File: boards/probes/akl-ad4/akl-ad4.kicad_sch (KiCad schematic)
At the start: 33 parts, among them J1 U.FL, J2 TIPRES, J3 TIPRES, J4 SMPM, U1 ADP7142ACPZN-R7, U2 ADP7182_DFN8, U3 LMR70503, U4 ADL5569

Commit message: Small tweaks to AKL-AD4 from design review. Ready for fab.
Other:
- company: (none) -> Antikernel Labs
- title: (none) -> AKL-AD4
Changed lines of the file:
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@@
 (kicad_sch (version 20211123) (generator eeschema)
   (paper "A4")
+  (title_block
+    (title "AKL-AD4")
+    (date "2022-06-11")
+    (rev "0.1")
+    (company "Antikernel Labs")
+    (comment 1 "Andrew D. Zonenberg")
+  )
   (junction (at 81.28 64.77) (diameter 0) (color 0 0 0 0)
   )

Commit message: Rev 0.2 of AKL-AD4
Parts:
- R7, R8: footprint azonenberg_pcb:EIA_0402_RES_NOSILK -> azonenberg_pcb:EIA_0201_RES_NOSILK
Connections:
- net 2V5_P: no longer U4.16 (PBDB)
- net GND: now also U4.16 (PBDB)
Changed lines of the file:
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@@
   (title_block
     (title "AKL-AD4")
-    (date "2022-06-11")
-    (rev "0.1")
+    (date "2022-06-24")
+    (rev "0.2")
     (company "Antikernel Labs")
     (comment 1 "Andrew D. Zonenberg")
@@
     (effects (font (size 1.27 1.27)) (justify right bottom))
   )
-  (label "2V5_P" (at 196.85 134.62 180)
+  (label "GND" (at 196.85 134.62 180)
     (effects (font (size 1.27 1.27)) (justify right bottom))
   )
@@
     (property "Reference" "R7" (id 0) (at 171.45 127 90))
     (property "Value" "348" (id 1) (at 171.45 129.54 90))
-    (property "Footprint" "azonenberg_pcb:EIA_0402_RES_NOSILK" (id 2) (at 171.45 131.318 90)
+    (property "Footprint" "azonenberg_pcb:EIA_0201_RES_NOSILK" (id 2) (at 171.45 131.318 90)
       (effects (font (size 1.27 1.27)) hide)
     )
@@
     (property "Reference" "R8" (id 0) (at 171.45 134.62 90))
     (property "Value" "348" (id 1) (at 171.45 132.08 90))
-    (property "Footprint" "azonenberg_pcb:EIA_0402_RES_NOSILK" (id 2) (at 171.45 133.858 90)
+    (property "Footprint" "azonenberg_pcb:EIA_0201_RES_NOSILK" (id 2) (at 171.45 133.858 90)
       (effects (font (size 1.27 1.27)) hide)
     )
@@
     )
     (path "/1063970e-8daf-483d-9d4f-e82ab2fd9360"
-      (reference "R7") (unit 1) (value "348") (footprint "azonenberg_pcb:EIA_0402_RES_NOSILK")
+      (reference "R7") (unit 1) (value "348") (footprint "azonenberg_pcb:EIA_0201_RES_NOSILK")
     )
     (path "/627fe034-b8ef-4aa6-bcef-25686ce4f366"
-      (reference "R8") (unit 1) (value "348") (footprint "azonenberg_pcb:EIA_0402_RES_NOSILK")
+      (reference "R8") (unit 1) (value "348") (footprint "azonenberg_pcb:EIA_0201_RES_NOSILK")
     )
     (path "/bc2ae153-e72d-4f62-822b-b8938bf03172"

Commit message: Updated AKL-AD4 v0.3
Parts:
- added C13: 0.47 uF, azonenberg_pcb:EIA_0402_CAP_NOSILK, symbol device:C
- added R12, R14: 470, azonenberg_pcb:EIA_0402_RES_NOSILK, symbol device:R
- added R13: 3312J-1-200E, azonenberg_pcb:RES_TRIM_BOURNS_3312, symbol device:POT_TRIM
- added U5: EQY-1-63+, azonenberg_pcb:DFN_8_0.5MM_2x2MM, symbol analog-azonenberg:EQY-x-63+
- J4: footprint azonenberg_pcb:CONN_SMPM_AMPHENOL_925-169J-51PT -> azonenberg_pcb:CONN_SMPM_AMPHENOL_925-169J-51PT_SHORT
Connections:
- net 2V5_N: now also R14.1
- net 2V5_P: now also R12.2
- net GND: now also C13.2, U5.1 (GND), U5.3 (NC/GND), U5.4 (NC/GND), U5.5 (NC/GND), U5.6 (NC/GND), U5.8 (GND), U5.PAD (GND); no longer U4.15 (VCOM)
- net VOUT: now also U5.2 (RF-IN); no longer J4.1 (In)
- new net: R12.1, R13.1
- new net: R13.3, R14.2
- new net VCOM: C13.1, R13.2, U4.15 (VCOM)
- new net VOUT_EQ: J4.1 (In), U5.7 (RF-OUT)
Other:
- note added: "100 ohm Zdiff +13 dB single ended gain from each leg -20 dB insertion loss from 10x probe Net gain through amplifier -7 dB or 2.24x attenuation But we actually see closer to -10 dB (3.16x): why?"
- note added: "VCOM input impedance is 2.5K ohm Assuming max +/- 100 mV in, that's 40 uA drawn by the input 470 + 20 + 470 = 960 ohms, 5.21 mA Pull range is +/- 10 ohms out of 960 = 52 mV"
- note removed: "100 ohm Zdiff +13 dB single ended gain from each leg -20 dB insertion loss from 10x probe Net gain -7 dB or 2.24x attenuation"
- moved on the sheet: C1, C10, C11, C12, C3, C4, C5, C7, C8, C9, J2, J3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

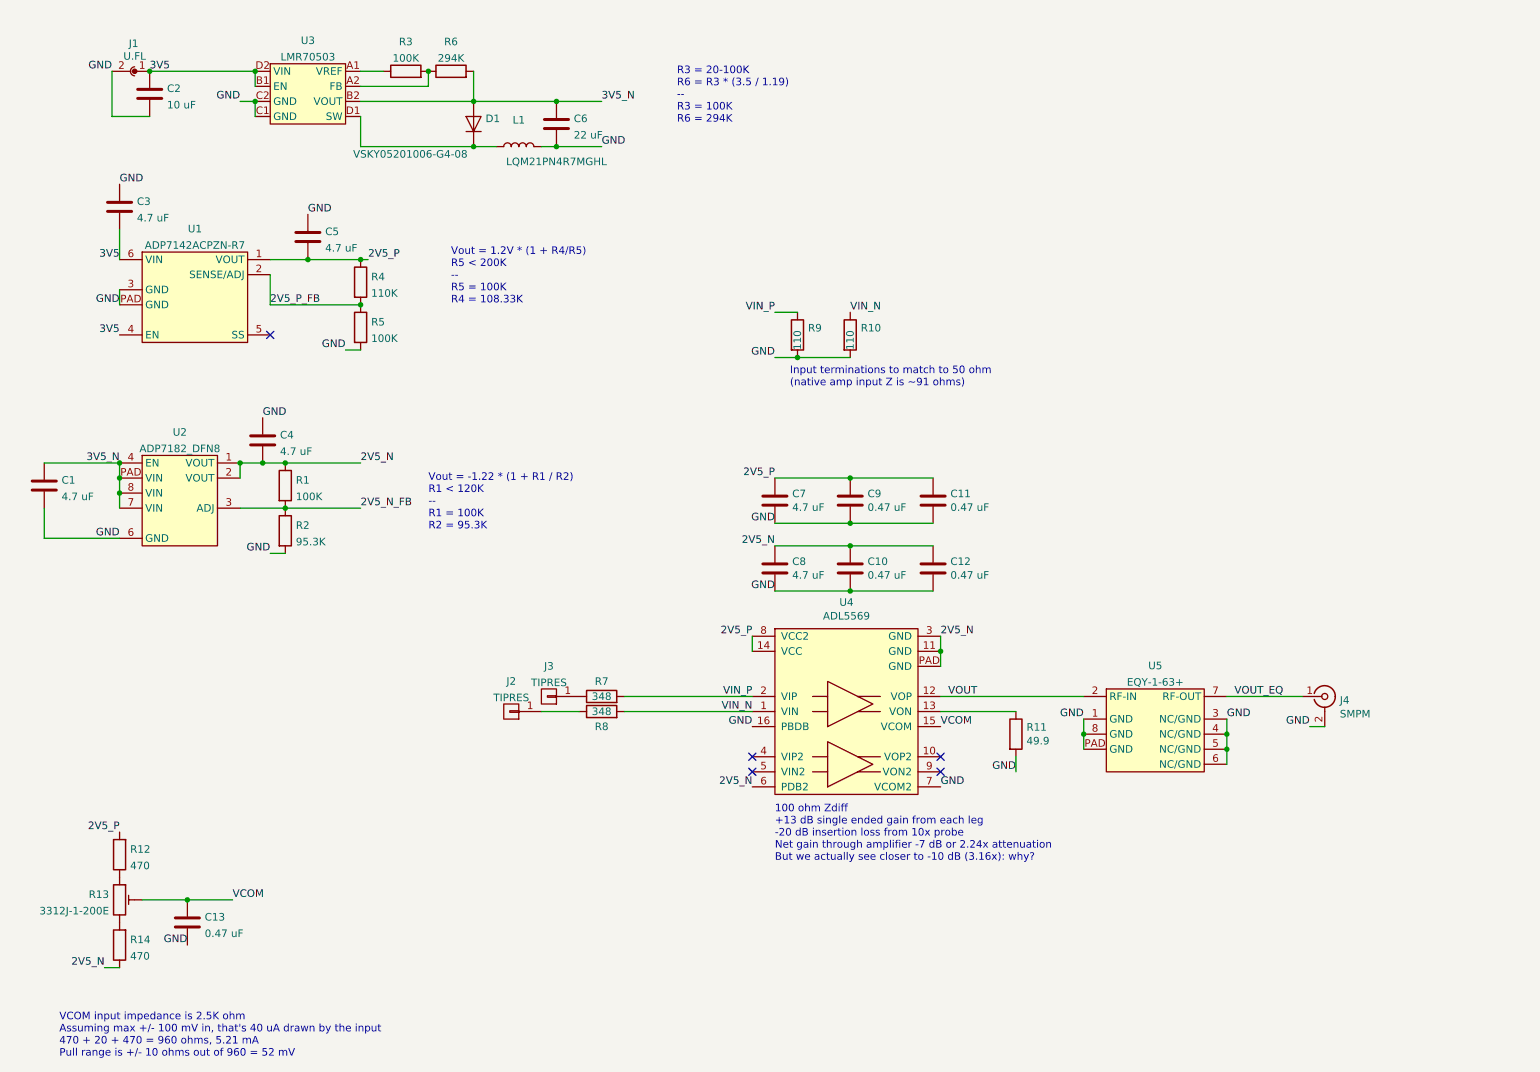
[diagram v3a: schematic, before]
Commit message: AKL-AD4: rev 0.4 with LM27761 based power stage, 2.5mm shorter, improved heatsinking, removed equalizer
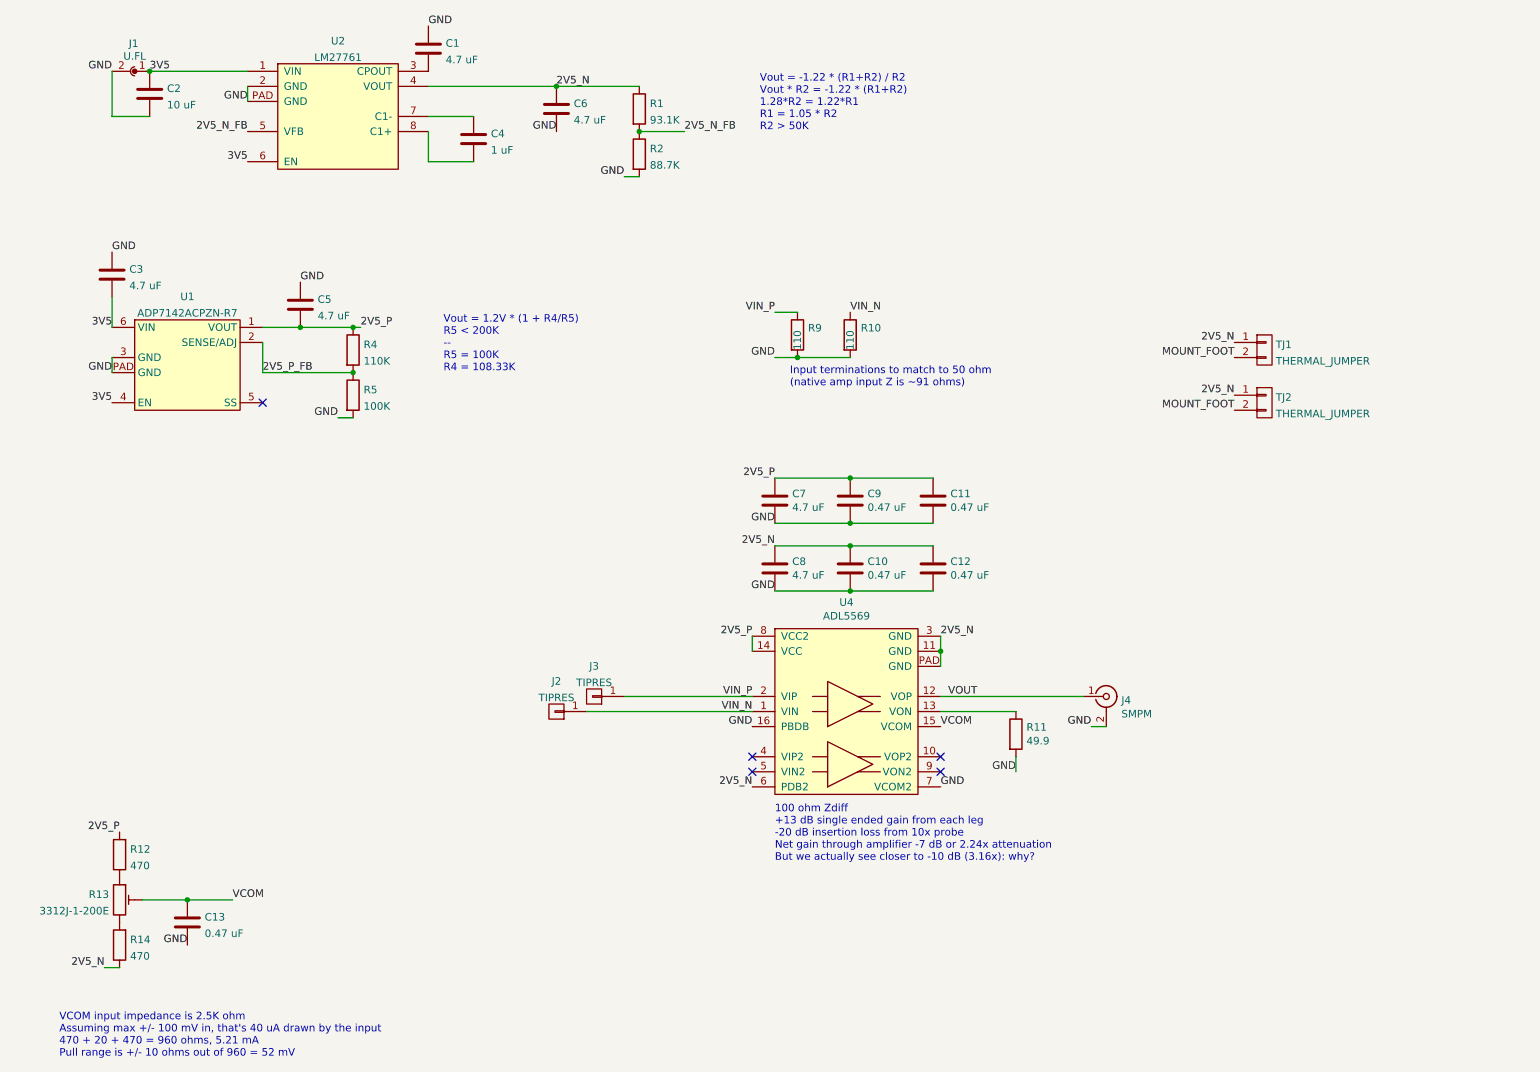
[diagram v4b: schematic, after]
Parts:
- removed D1: VSKY05201006-G4-08, azonenberg_pcb:EIA_0402_CAP_NOSILK, symbol device:D
- removed L1: LQM21PN4R7MGHL, azonenberg_pcb:EIA_0805_INDUCTOR_NOSILK, symbol device:L
- removed R3: 100K, azonenberg_pcb:EIA_0402_RES_NOSILK, symbol device:R
- removed R6: 294K, azonenberg_pcb:EIA_0402_RES_NOSILK, symbol device:R
- removed R7, R8: 348, azonenberg_pcb:EIA_0201_RES_NOSILK, symbol device:R
- removed U2: ADP7182_DFN8, azonenberg_pcb:DFN_8_0.5MM_3x3MM, symbol power-azonenberg:ADP7182_DFN8
- removed U3: LMR70503, azonenberg_pcb:BGA_8_1.65x0.865_0.4MM_TI_YFX, symbol power-azonenberg:LMR70503
- removed U5: EQY-1-63+, azonenberg_pcb:DFN_8_0.5MM_2x2MM, symbol analog-azonenberg:EQY-x-63+
- added TJ1, TJ2: THERMAL_JUMPER, azonenberg_pcb:EIA_0603_RES_NOSILK, symbol conn:CONN_01X02
- added U2: LM27761, azonenberg_pcb:DFN_8_0.5MM_2x2MM, symbol power-azonenberg:LM27761
- C4: value 4.7 uF -> 1 uF
- C6: value 22 uF -> 4.7 uF; footprint azonenberg_pcb:EIA_0805_CAP_NOSILK -> azonenberg_pcb:EIA_0603_CAP_NOSILK
- R1: value 100K -> 93.1K
- R2: value 95.3K -> 88.7K
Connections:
- net VOUT_EQ is gone; now on net VOUT: J4.1 (In)
- net 2V5_N: now also C6.1, TJ1.1 (P1), TJ2.1 (P1), U2.4 (VOUT); no longer C4.2
- net 2V5_N_FB: now also U2.5 (VFB)
- net 3V5: now also U2.1 (VIN), U2.6 (EN)
- net GND: now also C1.1, U2.2 (GND), U2.PAD (GND); no longer C1.2, C4.1
- net VIN_N: now also J2.1 (P1)
- net VIN_P: now also J3.1 (P1)
- removed net 3V5_N: C1.1, C6.1
- new net: C4.1, U2.7 (C1-)
- new net: C4.2, U2.8 (C1+)
- new net: C1.2, U2.3 (CPOUT)
- new net MOUNT_FOOT: TJ1.2 (P2), TJ2.2 (P2)
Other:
- note added: "Vout = -1.22 * (R1+R2) / R2 Vout * R2 = -1.22 * (R1+R2) 1.28*R2 = 1.22*R1 R1 = 1.05 * R2 R2 > 50K"
- note removed: "R3 = 20-100K R6 = R3 * (3.5 / 1.19) -- R3 = 100K R6 = 294K"
- note removed: "Vout = -1.22 * (1 + R1 / R2) R1 < 120K -- R1 = 100K R2 = 95.3K"
- moved on the sheet: C3, C5, J2, J3, J4, R4, R5, U1
